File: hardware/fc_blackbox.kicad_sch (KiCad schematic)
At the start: 3 parts

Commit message: Root sheet: place the sub-sheets; ESC as the 4in1 top sheet
esc_4in1.kicad_sch is OpenESC-20x20's 4in1-mini top sheet (battery input,
shunt and INA186 current sense, 12V/3V3 regulators, four ESC channel
instances). Its channel sub-sheet keeps its original file name ESC.kicad_sch
so the top sheet is untouched. Root sheet: Power, IMU, OSD, Blackbox, Pads,
RP2354A, ESC, RX placed, no wiring.
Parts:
- renumbered Card1 to Card2
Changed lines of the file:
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@@
 		)
 		(instances
-			(project "OpenFC"
-				(path "/fb88b6f9-ee39-4640-a9d4-04a17ceeac64/4c4f8c63-c695-4758-b1bc-c8af53273c68"
+			(project "OpenAIO"
+				(path "/fb88b6f9-ee39-4640-a9d4-04a17ceeac64/92d80a6e-4bd9-4df0-920d-da7b8cdc2925"
 					(reference "#PWR0155")
 					(unit 1)
@@
 		)
 		(instances
-			(project "OpenFC"
-				(path "/fb88b6f9-ee39-4640-a9d4-04a17ceeac64/4c4f8c63-c695-4758-b1bc-c8af53273c68"
+			(project "OpenAIO"
+				(path "/fb88b6f9-ee39-4640-a9d4-04a17ceeac64/92d80a6e-4bd9-4df0-920d-da7b8cdc2925"
 					(reference "R39")
 					(unit 1)
@@
 		(in_pos_files yes)
 		(dnp no)
-		(property "Reference" "Card1"
+		(property "Reference" "Card2"
 			(at 72.39 77.47 0)
 			(hide yes)
@@
 				)
 			)
-			(project "OpenFC"
-				(path "/fb88b6f9-ee39-4640-a9d4-04a17ceeac64/4c4f8c63-c695-4758-b1bc-c8af53273c68"
-					(reference "Card1")
+			(project "OpenAIO"
+				(path "/fb88b6f9-ee39-4640-a9d4-04a17ceeac64/92d80a6e-4bd9-4df0-920d-da7b8cdc2925"
+					(reference "Card2")
 					(unit 1)
 				)
@@
 		)
 		(instances
-			(project "OpenFC"
-				(path "/fb88b6f9-ee39-4640-a9d4-04a17ceeac64/4c4f8c63-c695-4758-b1bc-c8af53273c68"
+			(project "OpenAIO"
+				(path "/fb88b6f9-ee39-4640-a9d4-04a17ceeac64/92d80a6e-4bd9-4df0-920d-da7b8cdc2925"
 					(reference "#PWR060")
 					(unit 1)
@@
 		)
 		(instances
-			(project "OpenFC"
-				(path "/fb88b6f9-ee39-4640-a9d4-04a17ceeac64/4c4f8c63-c695-4758-b1bc-c8af53273c68"
+			(project "OpenAIO"
+				(path "/fb88b6f9-ee39-4640-a9d4-04a17ceeac64/92d80a6e-4bd9-4df0-920d-da7b8cdc2925"
 					(reference "#PWR0154")
 					(unit 1)
@@
 		)
 		(instances
-			(project "OpenFC"
-				(path "/fb88b6f9-ee39-4640-a9d4-04a17ceeac64/4c4f8c63-c695-4758-b1bc-c8af53273c68"
+			(project "OpenAIO"
+				(path "/fb88b6f9-ee39-4640-a9d4-04a17ceeac64/92d80a6e-4bd9-4df0-920d-da7b8cdc2925"
 					(reference "#PWR0153")
 					(unit 1)
@@
 		)
 		(instances
-			(project "OpenFC"
-				(path "/fb88b6f9-ee39-4640-a9d4-04a17ceeac64/4c4f8c63-c695-4758-b1bc-c8af53273c68"
+			(project "OpenAIO"
+				(path "/fb88b6f9-ee39-4640-a9d4-04a17ceeac64/92d80a6e-4bd9-4df0-920d-da7b8cdc2925"
 					(reference "C43")
 					(unit 1)

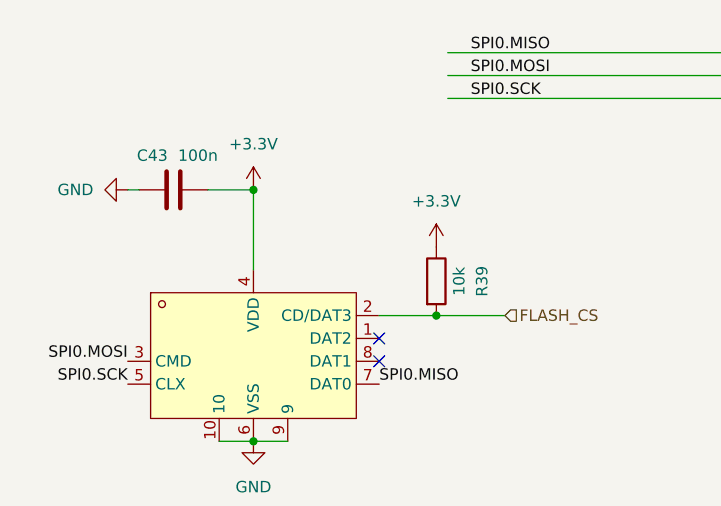
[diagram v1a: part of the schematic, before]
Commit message: Net classes: VBAT, Phase, Power, Gate, USB, RF, Analog with colours and patterns
Replaces the stale 50Ohm /ELRS/* patterns inherited from the template.
Widths and clearances start from the line standard (0.09/0.09, via 0.35/0.20)
and the ESC boards' practice; USB and RF geometry still to be checked against
the chosen JLCPCB 6-layer stackup.
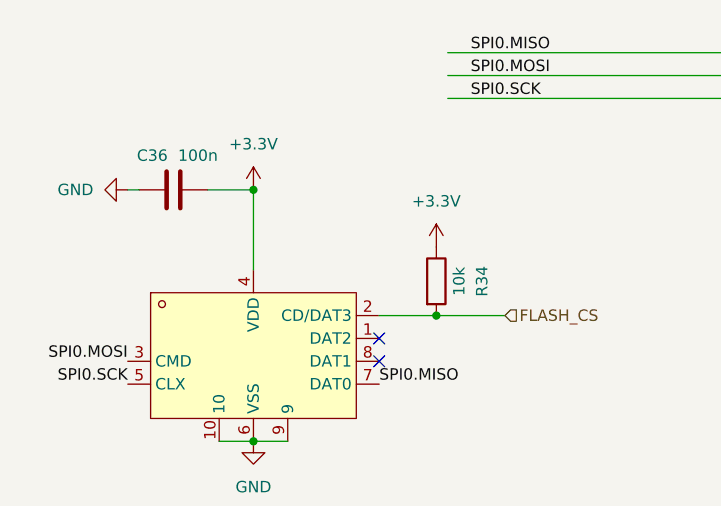
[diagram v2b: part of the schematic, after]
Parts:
- renumbered C43 to C36, Card2 to Card1, R39 to R34
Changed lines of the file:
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@@
 		(dnp no)
 		(fields_autoplaced yes)
-		(property "Reference" "#PWR0155"
+		(property "Reference" "#PWR0103"
 			(at 72.39 54.61 0)
 			(hide yes)
@@
 			(project "OpenAIO"
 				(path "/fb88b6f9-ee39-4640-a9d4-04a17ceeac64/92d80a6e-4bd9-4df0-920d-da7b8cdc2925"
-					(reference "#PWR0155")
+					(reference "#PWR0103")
 					(unit 1)
 				)
@@
 		(in_pos_files yes)
 		(dnp no)
-		(property "Reference" "R39"
+		(property "Reference" "R34"
 			(at 97.79 60.96 90)
 			(show_name no)
@@
 			(project "OpenAIO"
 				(path "/fb88b6f9-ee39-4640-a9d4-04a17ceeac64/92d80a6e-4bd9-4df0-920d-da7b8cdc2925"
-					(reference "R39")
+					(reference "R34")
 					(unit 1)
 				)
@@
 		(in_pos_files yes)
 		(dnp no)
-		(property "Reference" "Card2"
+		(property "Reference" "Card1"
 			(at 72.39 77.47 0)
 			(hide yes)
@@
 			(project "OpenAIO"
 				(path "/fb88b6f9-ee39-4640-a9d4-04a17ceeac64/92d80a6e-4bd9-4df0-920d-da7b8cdc2925"
-					(reference "Card2")
+					(reference "Card1")
 					(unit 1)
 				)
@@
 		(dnp no)
 		(fields_autoplaced yes)
-		(property "Reference" "#PWR060"
+		(property "Reference" "#PWR0102"
 			(at 52.07 50.8 0)
 			(hide yes)
@@
 			(project "OpenAIO"
 				(path "/fb88b6f9-ee39-4640-a9d4-04a17ceeac64/92d80a6e-4bd9-4df0-920d-da7b8cdc2925"
-					(reference "#PWR060")
+					(reference "#PWR0102")
 					(unit 1)
 				)
@@
 		(dnp no)
 		(fields_autoplaced yes)
-		(property "Reference" "#PWR0154"
+		(property "Reference" "#PWR0104"
 			(at 72.39 85.09 0)
 			(hide yes)
@@
 			(project "OpenAIO"
 				(path "/fb88b6f9-ee39-4640-a9d4-04a17ceeac64/92d80a6e-4bd9-4df0-920d-da7b8cdc2925"
-					(reference "#PWR0154")
+					(reference "#PWR0104")
 					(unit 1)
 				)
@@
 		(dnp no)
 		(fields_autoplaced yes)
-		(property "Reference" "#PWR0153"
+		(property "Reference" "#PWR0105"
 			(at 92.71 60.96 0)
 			(hide yes)
@@
 			(project "OpenAIO"
 				(path "/fb88b6f9-ee39-4640-a9d4-04a17ceeac64/92d80a6e-4bd9-4df0-920d-da7b8cdc2925"
-					(reference "#PWR0153")
+					(reference "#PWR0105")
 					(unit 1)
 				)
@@
 		(in_pos_files yes)
 		(dnp no)
-		(property "Reference" "C43"
+		(property "Reference" "C36"
 			(at 59.436 46.99 90)
 			(show_name no)
@@
 			(project "OpenAIO"
 				(path "/fb88b6f9-ee39-4640-a9d4-04a17ceeac64/92d80a6e-4bd9-4df0-920d-da7b8cdc2925"
-					(reference "C43")
-					(unit 1)
-				)
+					(reference "C36")
+					(unit 1)
+				)

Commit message: OpenAIO: master PCB with Base and Core islands routed, AIO_outline footprint+symbol in project lib
Save point before the two-board (LGA) split tooling.
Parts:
- C36, R34: KiLib_Generator (none) -> SMD_2terminal_chip_molded
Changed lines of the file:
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@@
+			)
+		)
+		(property "KiLib_Generator" "SMD_2terminal_chip_molded"
+			(at 92.71 60.96 0)
+			(hide yes)
+			(show_name no)
+			(do_not_autoplace no)
+			(effects
+				(font
+					(size 1.27 1.27)
+				)
 			)
 		)
@@
 			(hide yes)
 			(show_name no)
+			(do_not_autoplace no)
+			(effects
+				(font
+					(size 1.27 1.27)
+				)
+			)
+		)
+		(property "KiLib_Generator" "SMD_2terminal_chip_molded"
+			(at 63.5 50.8 0)
+			(hide yes)
+			(show_name no)
